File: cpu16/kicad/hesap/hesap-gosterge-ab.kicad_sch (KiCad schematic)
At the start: 40 parts, among them U185 74HC08, U186 74HC32, U187 74HC02, U188 74HC04, U189 74HC4511, U190 74HC4511, U191 74HC4511, U192 74HC08, U193 74HC32, U194 74HC02, U195 74HC04, U196 74HC4511, U197 74HC4511, U198 74HC4511

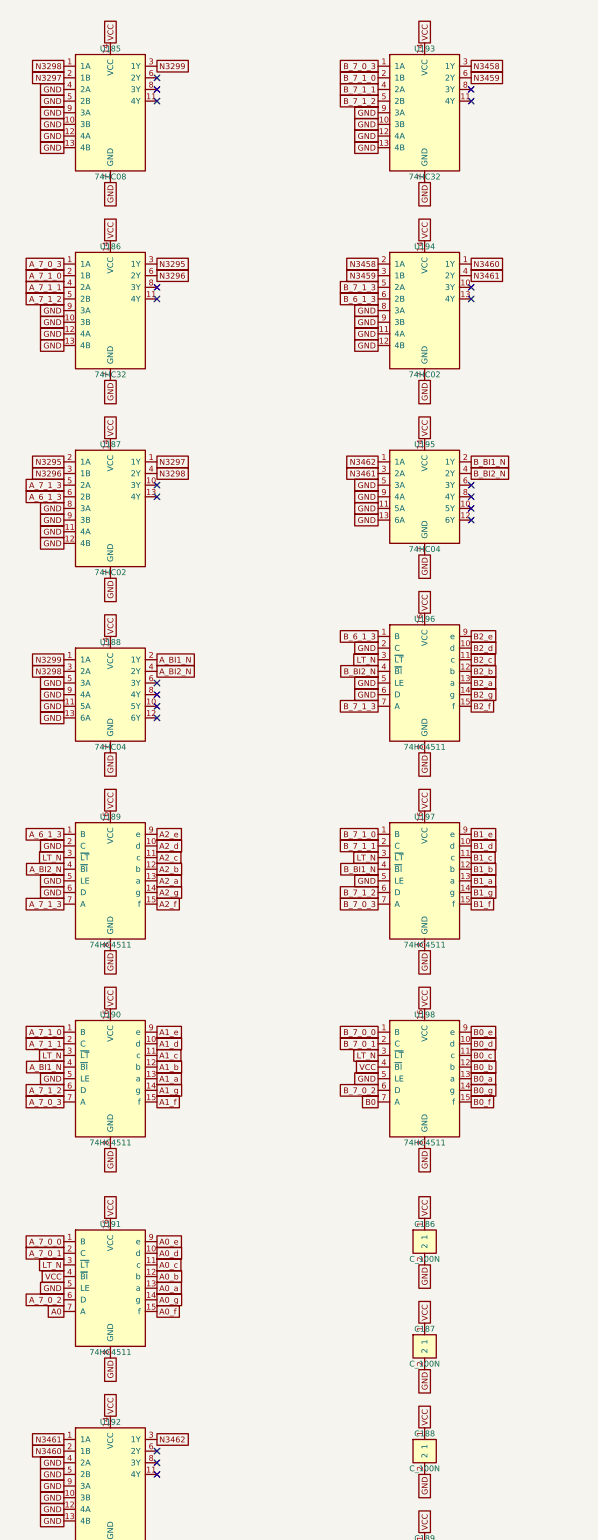
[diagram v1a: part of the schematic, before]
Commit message: Hesap makinesi: eksi işareti sonucun solunda, lamba testinde de yanar; HATA LED'i göstergelerin yanında
- işaret hanesi (DS7) sonucun hanelerinden önce yerleşir: 3D kartta ve
  şemada en solda
- ISARET_g = NEG + lamba testi (boş kapı birimleriyle, çip sayısı aynı)
- HATA LED'i Bölme bloğundan "Gösterge: Sonuç" bloğuna
- rehber ve tasarım belgesi güncellendi

Co-Authored-By: Claude Opus 5.5 (1M context) <noreply@anthropic.com>
Claude-Session: https://claude.ai/code/session_018J8WVuECVRbQJyCbmF6Nsi
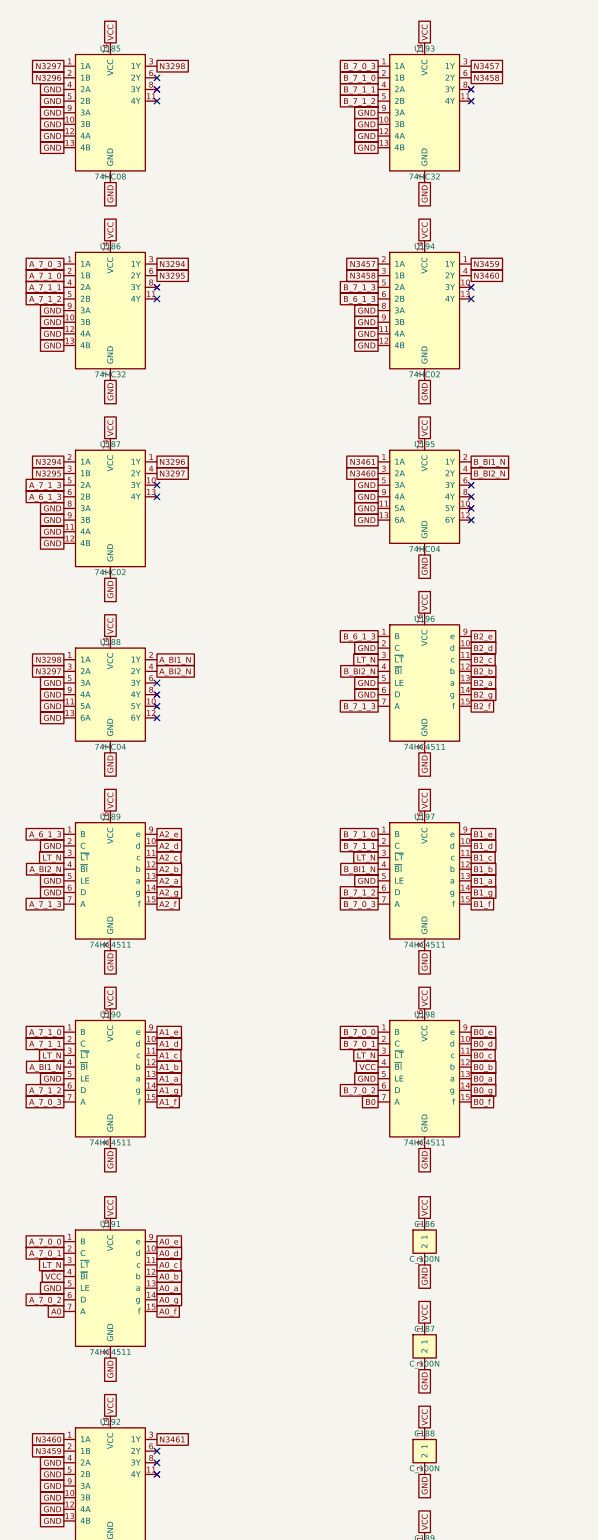
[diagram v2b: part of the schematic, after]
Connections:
- net N3299 is gone; now on net N3298: U185.3 (1Y), U188.1 (1A)
- net N3462 is gone; now on net N3461: U192.3 (1Y), U195.1 (1A)
- net N3295: now also U186.6 (2Y), U187.3 (1B); no longer U186.3 (1Y), U187.2 (1A)
- net N3296: now also U185.2 (1B), U187.1 (1Y); no longer U186.6 (2Y), U187.3 (1B)
- net N3297: now also U185.1 (1A), U187.4 (2Y), U188.3 (2A); no longer U185.2 (1B), U187.1 (1Y)
- net N3298: no longer U185.1 (1A), U187.4 (2Y), U188.3 (2A)
- net N3458: now also U193.6 (2Y), U194.3 (1B); no longer U193.3 (1Y), U194.2 (1A)
- net N3459: now also U192.2 (1B), U194.1 (1Y); no longer U193.6 (2Y), U194.3 (1B)
- net N3460: now also U192.1 (1A), U194.4 (2Y), U195.3 (2A); no longer U192.2 (1B), U194.1 (1Y)
- net N3461: no longer U192.1 (1A), U194.4 (2Y), U195.3 (2A)
- new net N3294: U186.3 (1Y), U187.2 (1A)
- new net N3457: U193.3 (1Y), U194.2 (1A)
